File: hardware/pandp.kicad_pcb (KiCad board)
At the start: 2 copper layers, 116 x 55.5 mm, 92 parts, among them IC1 ADP2303-5, P1 CONN_01X02, P10 CONN_01X04, P11 CONN_01X02, P12 CONN_02X04, P13 CONN_01X02, P14 CONN_01X04, P15 CONN_01X04, P16 CONN_01X03, P17 CONN_01X03, P18 CONN_01X03, P19 CONN_01X03, P2 CONN_01X03, P20 CONN_01X03, P21 CONN_01X03, P22 CONN_02X03, P23 CONN_02X03, P24 CONN_02X03, P25 CONN_02X03, P26 CONN_01X03, P27 CONN_01X03, P28 CONN_01X03, P29 CONN_01X03, P3 CONN_01X02, P30 CONN_01X04, P31 CONN_01X04, P32 CONN_01X04, P33 CONN_01X04, P4 CONN_01X03, P6 CONN_01X03, P7 CONN_01X03, P8 USB_OTG, P9 CONN_01X02, Q1 IRF540N, Q2 IRF540N, SW1 SW_PUSH, U1 AP1117D33, U2 STM32F103RC, Y1 Crystal_Small - 2101357 on el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, Y2 Crystal_Small - 2063972 on el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

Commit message: minor change to board text
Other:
- board text added: "PaPaPaR - v1 - Takigama me@pjr.cc https://github.com/takigama/PaPaPaR"
- board text removed: "PaPaPaR - v1 - Takigama me@pjr.cc"
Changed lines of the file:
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@@
   (page A4)
   (layers
-    (0 F.Cu signal)
-    (31 B.Cu signal)
+    (0 F.Cu signal hide)
+    (31 B.Cu signal hide)
     (32 B.Adhes user)
     (33 F.Adhes user)
@@
     (effects (font (size 1.5 1.5) (thickness 0.3)))
   )
-  (gr_text "PaPaPaR - v1 - Takigama\nme@pjr.cc" (at 145.25 96 20) (layer B.SilkS)
+  (gr_text "PaPaPaR - v1 - Takigama\nme@pjr.cc\nhttps://github.com/takigama/PaPaPaR" (at 143.75 93 7) (layer B.SilkS)
     (effects (font (size 2.8 2.8) (thickness 0.3)) (justify mirror))
   )

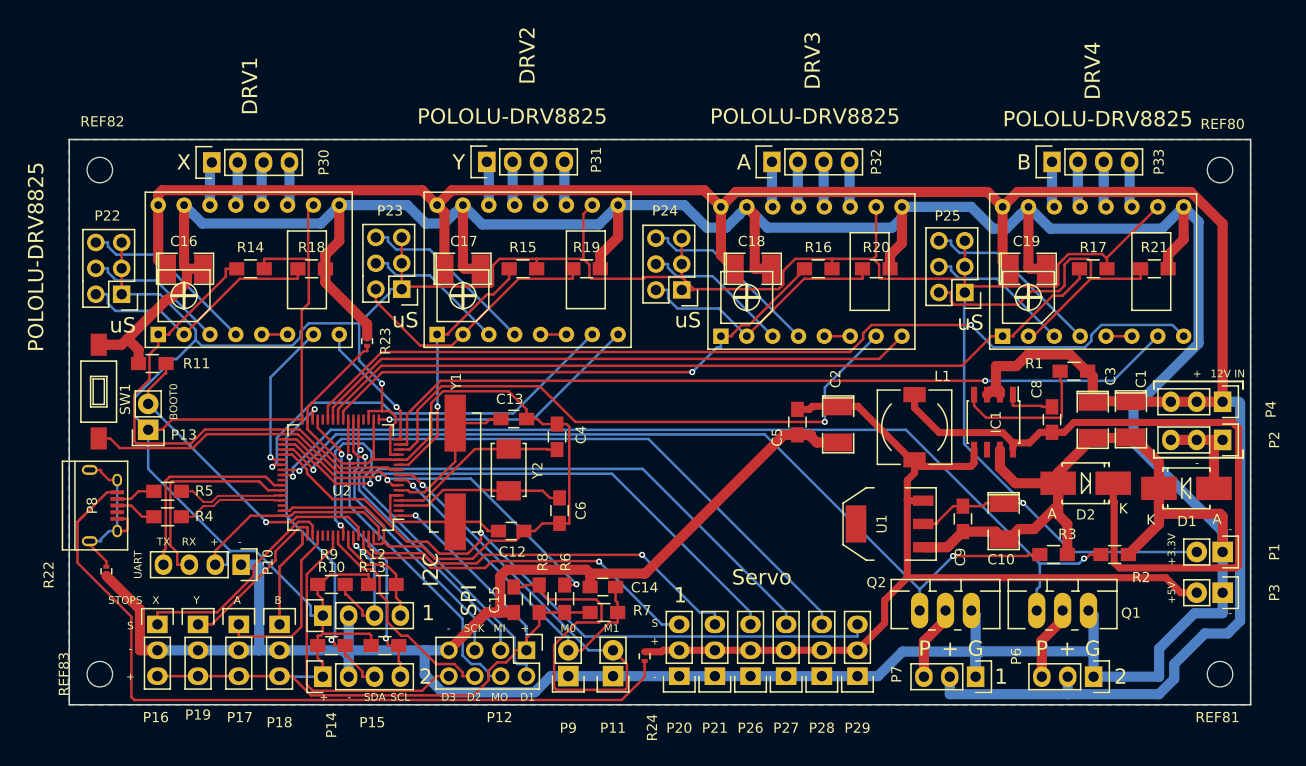
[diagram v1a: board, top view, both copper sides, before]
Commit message: added 5v dc motor control - low current - 500ma or less
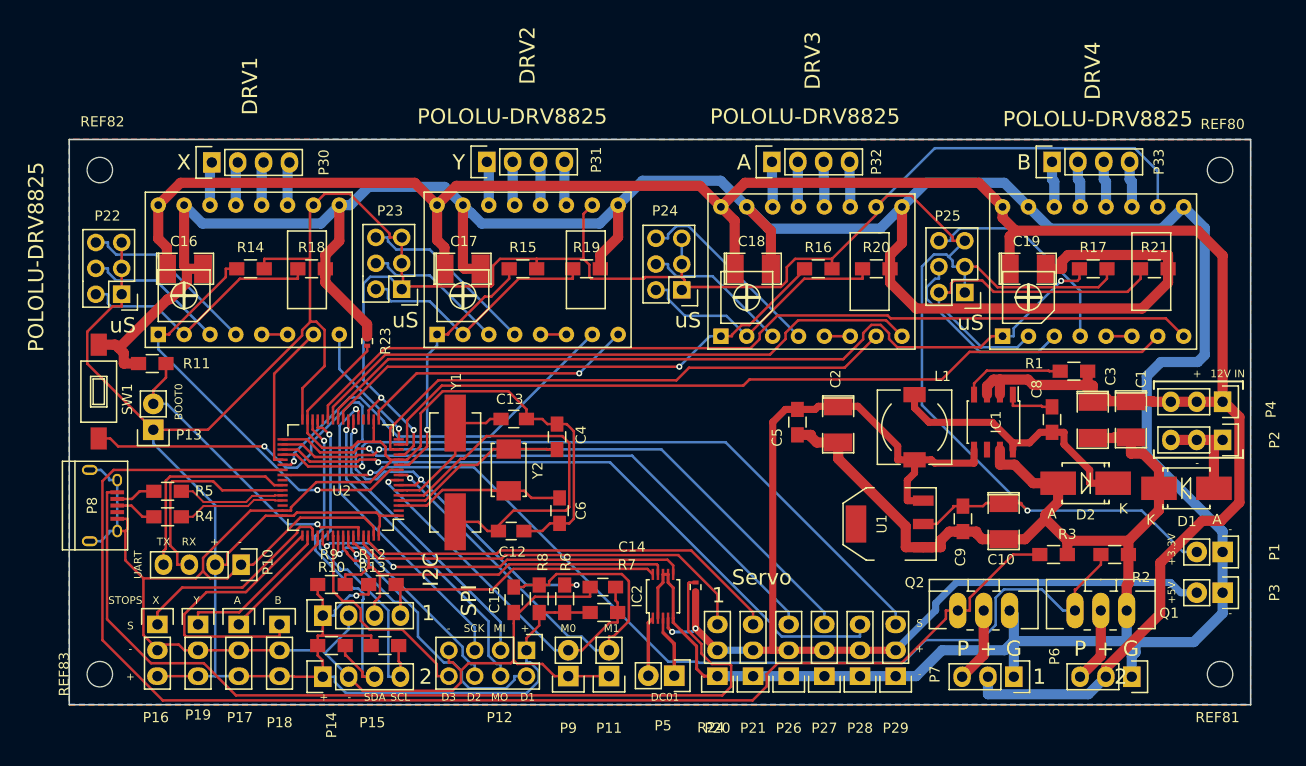
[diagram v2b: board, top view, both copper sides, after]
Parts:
- removed R22: R, Resistors_SMD:R_0402
- added IC2: DRV8830, Housings_SSOP:TSSOP-10_3x3mm_Pitch0.5mm, F.Cu at (140.8, 106.6)
- added P5: CONN_01X02, Pin_Headers:Pin_Header_Straight_1x02, F.Cu at (141.9, 114.4)
- moved R24 8.44 mm to (144.0, 105.7), turned to 270 degrees
- moved P20 3.75 mm to (146.1, 114.4)
- moved P21 3.75 mm to (149.6, 114.4)
- moved P26 3.75 mm to (153.1, 114.4)
- moved P27 3.75 mm to (156.6, 114.4)
- moved P28 3.75 mm to (160.1, 114.4)
- moved P29 3.75 mm to (163.6, 114.4)
- moved P6 3.75 mm to (186.8, 114.5)
- moved P7 3.75 mm to (175.2, 114.5)
- moved Q1 3.75 mm to (183.8, 108.0)
- moved Q2 3.75 mm to (172.3, 108.0)
- moved P13 0.50 mm to (90.8, 90.2)
- moved P11 0.40 mm to (135.5, 114.4)
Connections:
- C14 pad 2: GND -> GNDD
- C15 pad 2: GND -> GNDD
- P10 pad 1: GND -> GNDD
- P11 pad 1: GND -> GNDD
- P12 pad 7: GND -> GNDD
- P14 pad 2: GND -> GNDD
- P15 pad 2: GND -> GNDD
- P16 pad 2: GND -> GNDD
- P17 pad 2: GND -> GNDD
- P18 pad 2: GND -> GNDD
- P19 pad 2: GND -> GNDD
- P8 pad 5: GNDA -> GNDD
- P8 pad 6: GNDA -> GNDD
- P9 pad 1: GND -> GNDD
- U2 pad 53: (no net) -> FAULTn
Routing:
- net GNDD: track 92.9 -> 211.1 mm
- net GND: track 519.7 -> 435.9 mm
- net CONT_1: track 85.7 -> 136.1 mm, vias 2 -> 0
- net Net-(C8-Pad2): track 70.1 -> 26.8 mm
- net FAULTn: track 0.00 -> 37.8 mm, vias 0 -> 2
- net SCL_1: track 11.1 -> 39.5 mm, vias 0 -> 1
- net SDA_1: track 13.8 -> 41.7 mm, vias 1 -> 0
- net OSC_OUT: track 14.3 -> 38.8 mm
- net +5V: track 93.8 -> 114.4 mm, vias 0 -> 2
- net END_A: track 9.65 -> 27.4 mm
- net GNDA: track 17.7 -> 0.00 mm
- net +12V: track 243.9 -> 228.9 mm
- net GD1: track 42.3 -> 27.7 mm
- net +5VL: track 78.4 -> 91.9 mm
- net MEASURE_1: track 61.1 -> 48.0 mm
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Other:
- net class motor added: clearance 0.2, trace_width 0.35, via_dia 0.6, via_drill 0.4
- board text added: "DC01"
